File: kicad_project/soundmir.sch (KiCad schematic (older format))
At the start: 21 parts, among them P1 CONN_01X04, P2 CONN_01X04, P3 CONN_01X02, P4 CONN_01X02, Q1 PN2222A, Q2 PN2222A, U1 microstack_gps, U2 i2c_logic_lvl_converter, U3 Raspberry_Pi_2_3, U4 a4988_module, U5 boost_converter

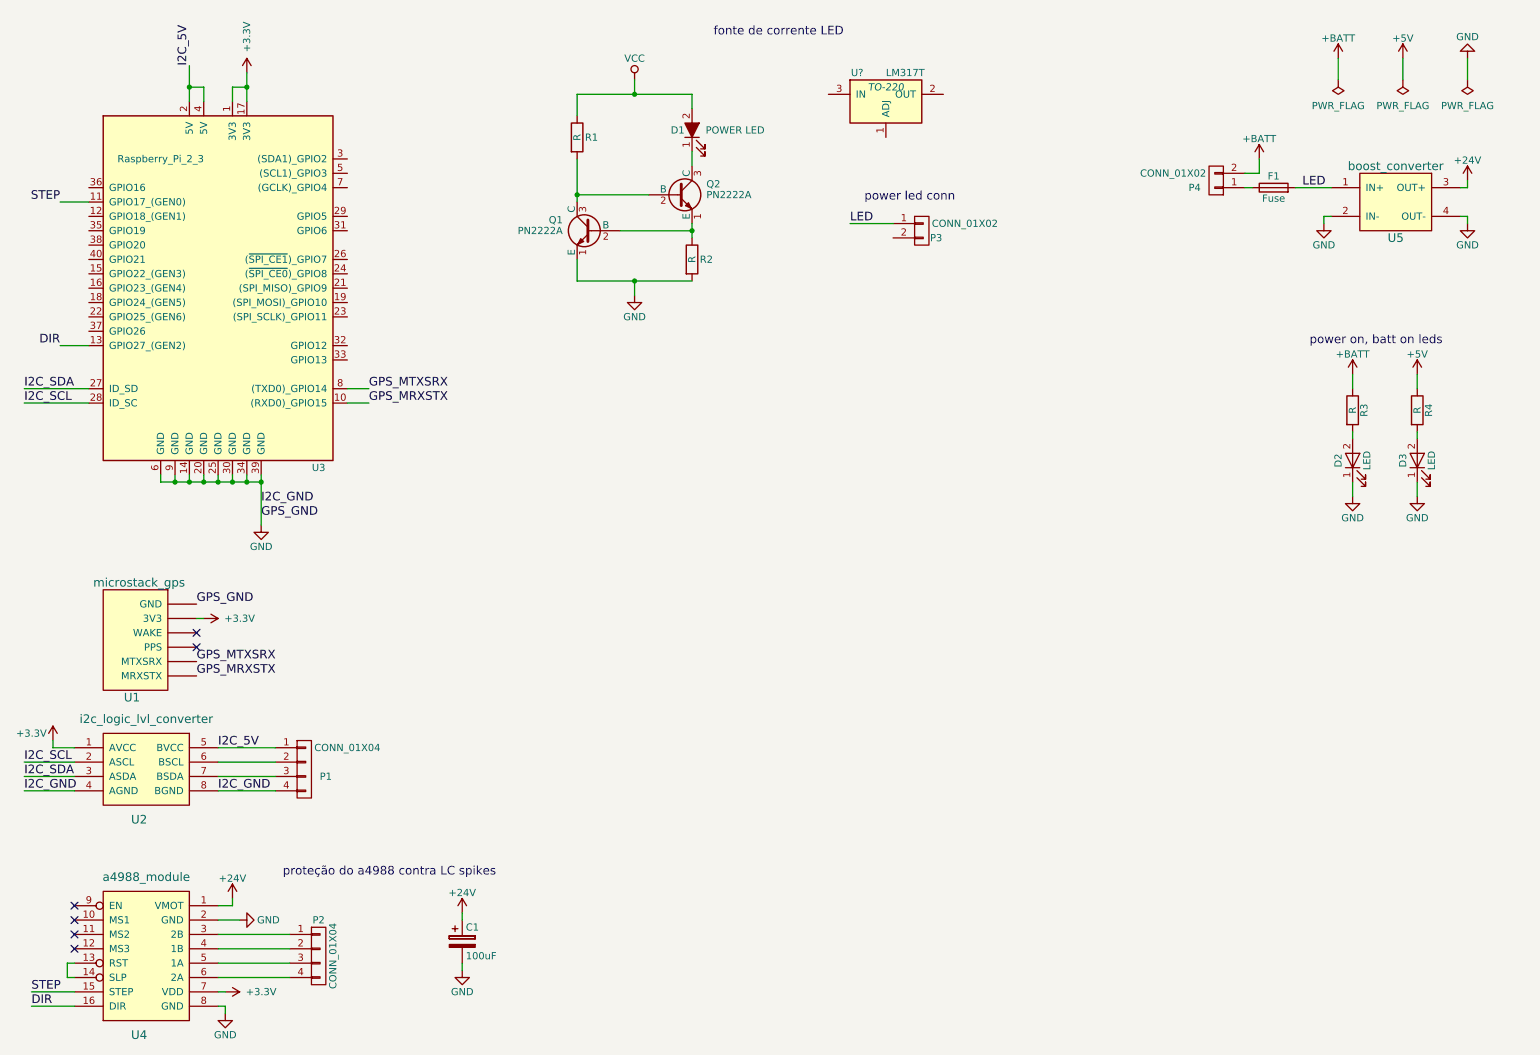
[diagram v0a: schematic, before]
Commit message: alimentação, acelerometro, leds indicadores
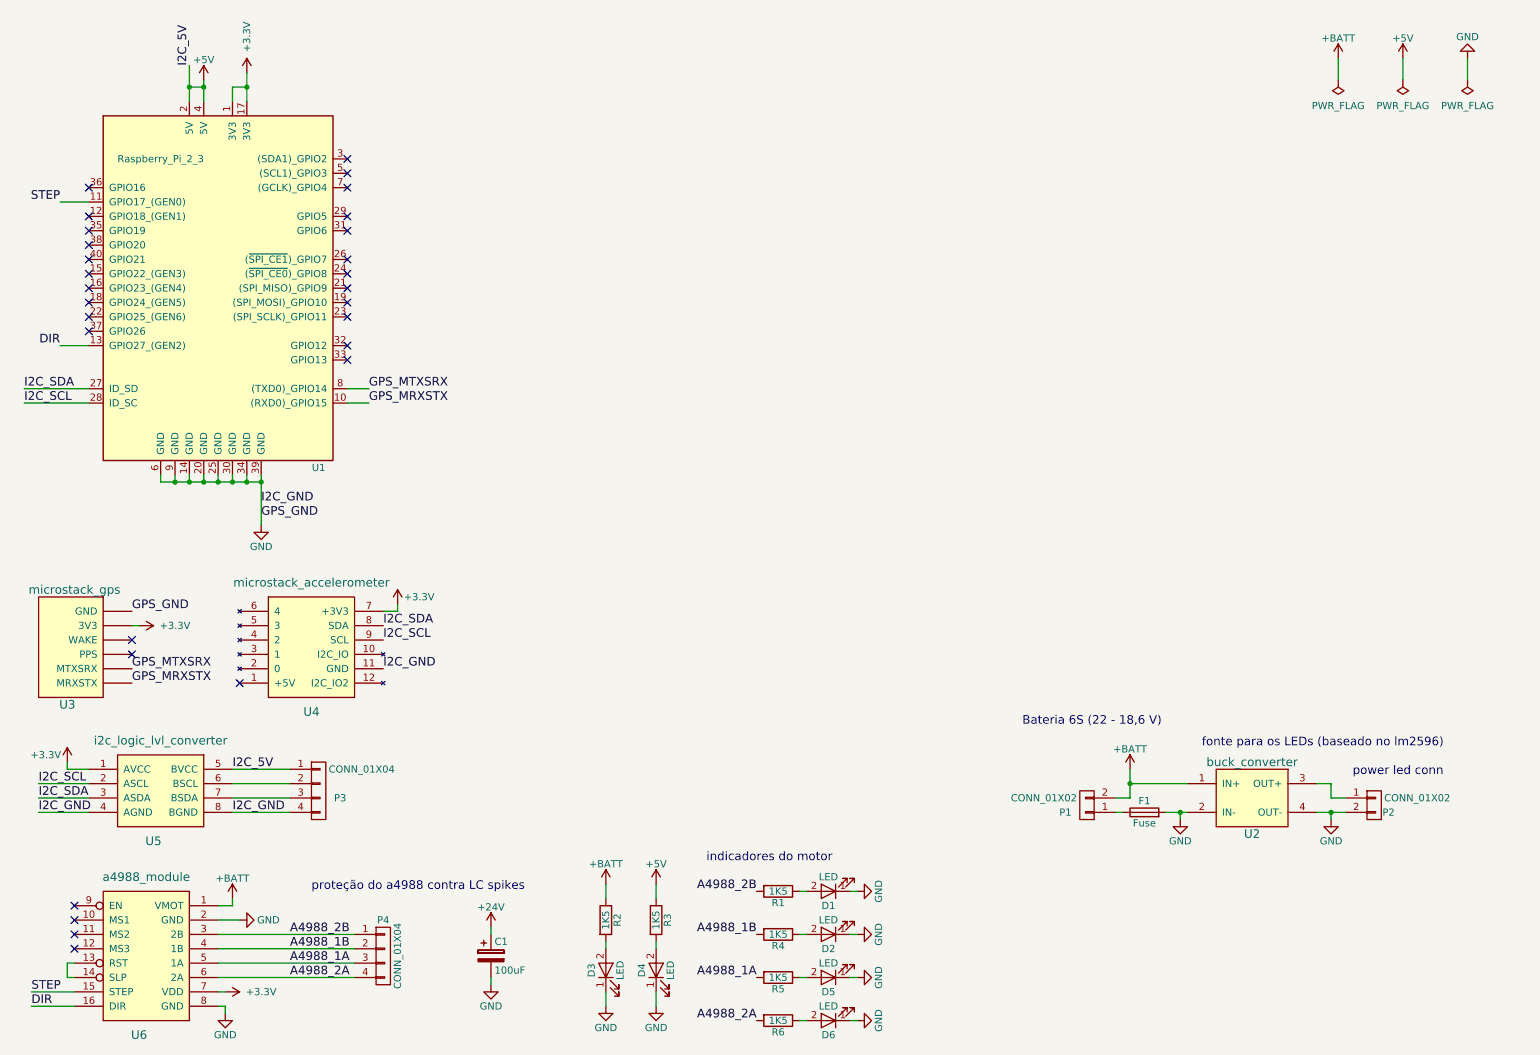
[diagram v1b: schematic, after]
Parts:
- removed D1: POWER LED, symbol LED_ALT
- removed Q1, Q2: PN2222A, symbol PN2222A
- removed R2: R, symbol R
- removed U?: LM317T, TO-220, symbol LM317T
- added D1, D2, D5, D6: LED, symbol LED
- added R4, R5, R6: 1K5, symbol R
- added U4: microstack_accelerometer, symbol microstack_accelerometer
- R1: value R -> 1K5
- R2: renamed from R3; value R -> 1K5
- R3: renamed from R4; value R -> 1K5
- U2: renamed from U5; value boost_converter -> buck_converter
- renumbered D2 to D3, D3 to D4, P4 to P1, P3 to P2, P1 to P3, P2 to P4, U3 to U1, U1 to U3, U2 to U5, U4 to U6
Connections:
- net I2C_5V is gone; now on net +5V: P3.1 (P1), U1.2 (5V), U1.4 (5V), U5.5 (BVCC)
- net +24V: no longer U2.3 (OUT+), U6.1 (VMOT)
- net +3V3: now also U4.7 (+3V3)
- net +BATT: now also U2.1 (IN+), U6.1 (VMOT)
- net GND: now also F1.2, P2.2 (P2), D1.1 (K), D2.1 (K), D5.1 (K), D6.1 (K), U4.11 (GND)
- net I2C_SCL: now also U4.9 (SCL)
- net I2C_SDA: now also U4.8 (SDA)
- net A4988_2B: now reaches P4.1 (P1), U6.3 (2B)
- net A4988_2B: now also R1.2
- net A4988_1B: now reaches P4.2 (P2), U6.4 (1B)
- net A4988_1B: now also R4.2
- net A4988_1A: now reaches P4.3 (P3), U6.5 (1A)
- net A4988_1A: now also R5.2
- net A4988_2A: now reaches P4.4 (P4), U6.6 (2A)
- net A4988_2A: now also R6.2
- removed net LED: F1.2, P2.1 (P1), U2.1 (IN+)
- net VCC: no longer names the net of R1.1
- net VCC: now also D1.2 (A)
- new net: P2.1 (P1), U2.3 (OUT+)
- new net: D6.2 (A), R6.1
- new net: D5.2 (A), R5.1
- new net: D2.2 (A), R4.1
- no-connect marks 6 -> 29
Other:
- note added: "Bateria 6S (22 - 18,6 V)"
- note added: "fonte para os LEDs (baseado no lm2596)"
- note added: "indicadores do motor"
- note removed: "fonte de corrente LED"
- note removed: "power on, batt on leds"
- moved on the sheet: C1, D3, D4, F1, P1, P2, P3, P4, R2, R3, U2, U3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

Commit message: terminado esquematico, talvez
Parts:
- added C1, C2: 2u2, symbol C
- added C?: 100uF, symbol CP
- added J1: JACK_TRS_6PINS, symbol JACK_TRS_6PINS
- added P1: CONN_01X03, symbol CONN_01X03
- added R1, R4: 100K, symbol R
- added R2, R5: 50, symbol R
- added R3, R6: 1k, symbol R
- added RV1, RV2, RV3, RV4: POT_TRIM 100k, symbol POT_TRIM
- added U2: NE5532, symbol NE5532
- added W? (x17): TEST_1P, symbol TEST_1P
- renumbered C1 to C3, P3 to P2, P1 to P3, P2 to P4, P4 to P5, R4 to R10, R5 to R11, R6 to R12, R1 to R7, R2 to R8, R3 to R9, U2 to U6, U6 to U7
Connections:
- net +24V is gone; now on net +BATT: C3.1
- net +3V3: no longer U1.1 (3V3)
- net +5V: now also C?.1, R1.1, R4.1, U2.8 (V+), U2.8 (V+), W?.1; no longer P2.1 (P1), U1.2 (5V), U5.5 (BVCC)
- net +BATT: now also W?.1
- net A4988_1A: now also W?.1
- net A4988_1B: now also W?.1
- net A4988_2A: now also W?.1
- net A4988_2B: now also W?.1
- net DIR: now also W?.1
- net GND: now also C?.2, J1.1 (S), P1.3 (P3), R3.2, R6.2, RV1.1, RV3.1, U2.4 (V-), U2.4 (V-), W?.1, W?.1
- net I2C_SCL: now also W?.1
- net I2C_SDA: now also W?.1
- net STEP: now also W?.1
- net at P4.1 (P1), U6.3 (OUT+): now also W?.1
- new net: R6.1, RV4.1, U2.6 (-)
- new net: R5.2, RV4.2, U2.7
- new net: C2.2, R5.1
- new net: R2.2, RV2.2, U2.1
- new net: R3.1, RV2.1, U2.2 (-)
- new net: C1.2, R2.1
- new net I2C_5V: P2.1 (P1), U1.2 (5V), U5.5 (BVCC)
- new net L_AUDIO_IN: J1.2 (T), R1.2, RV1.2, U2.3 (+), W?.1
- new net L_AUDIO_OUT: C1.1, P1.1 (P1), W?.1
- new net R_AUDIO_IN: J1.3 (R), R4.2, RV3.2, U2.5 (+), W?.1
- new net R_AUDIO_OUT: C2.1, P1.2 (P2), W?.1
- no-connect marks 29 -> 36
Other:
- note added: "NE5532 bypass cap"
- moved on the sheet: C3

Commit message: DRC realizada
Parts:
- gave numbers to parts that had none: 18
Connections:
- net +3V3: now also U1.1 (3V3)
